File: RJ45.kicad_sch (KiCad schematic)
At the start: 5 parts, among them J9 RJ45_LED_Shielded

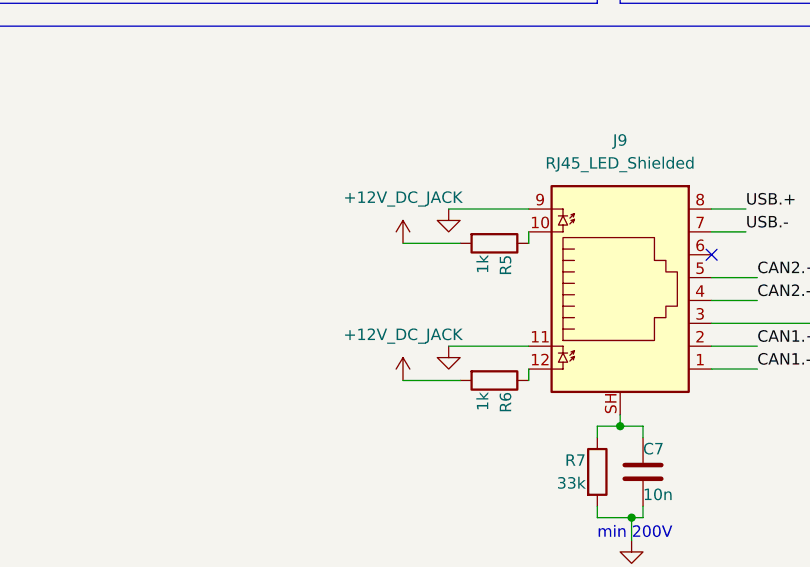
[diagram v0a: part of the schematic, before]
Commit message: Change power source
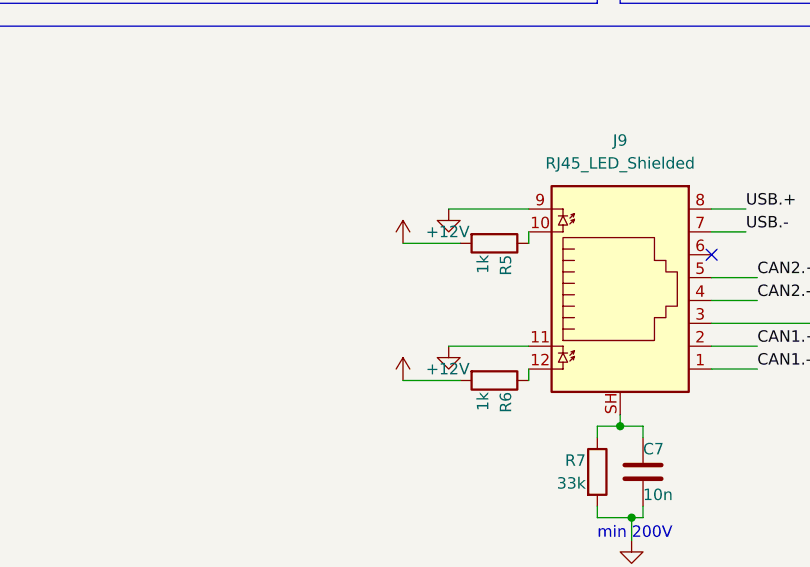
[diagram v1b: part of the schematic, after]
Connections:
- net +12V_DC_JACK renamed +12V
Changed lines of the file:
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@@
 			)
 		)
-		(property "Value" "+12V_DC_JACK"
-			(at 121.92 120.65 0)
+		(property "Value" "+12V"
+			(at 124.46 124.4599 0)
 			(effects
 				(font
 					(size 1.27 1.27)
 				)
+				(justify left)
 			)
 		)
@@
 			)
 		)
-		(property "Value" "+12V_DC_JACK"
-			(at 121.92 105.41 0)
+		(property "Value" "+12V"
+			(at 124.46 109.2199 0)
 			(effects
 				(font
 					(size 1.27 1.27)
 				)
+				(justify left)
 			)
 		)

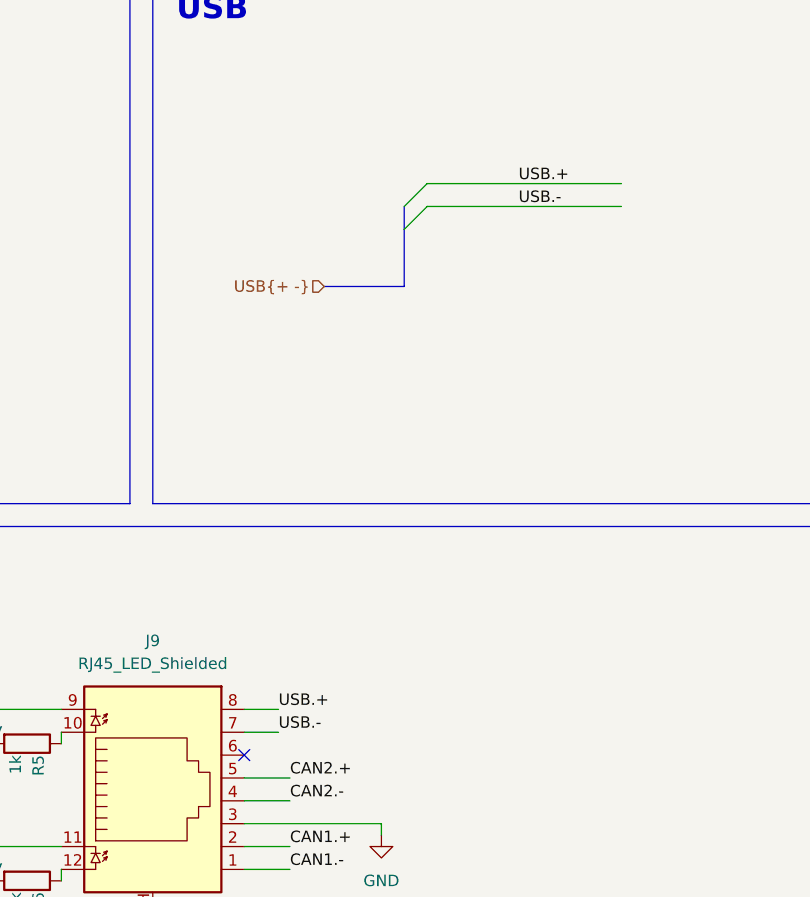
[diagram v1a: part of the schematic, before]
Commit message: Change USB net names
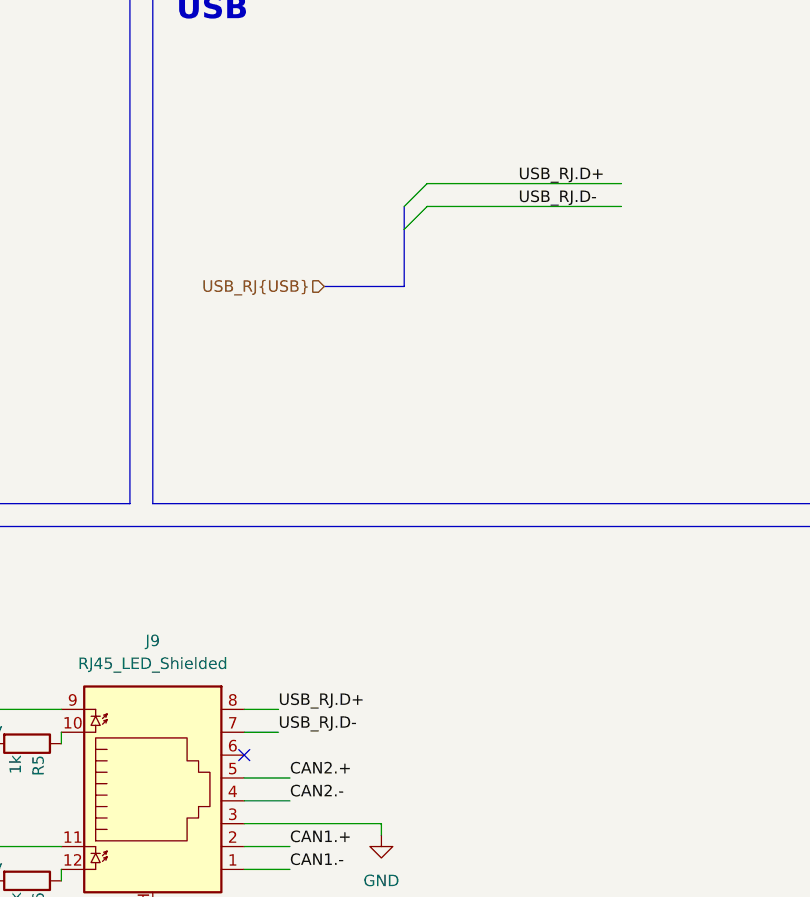
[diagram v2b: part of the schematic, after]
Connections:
- net USB.+ renamed USB_RJ.D+
- net USB.- renamed USB_RJ.D-
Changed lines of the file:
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@@
 		)
 	)
-	(label "USB.+"
+	(label "USB_RJ.D+"
 		(at 186.69 48.26 0)
 		(effects
@@
 		)
 	)
-	(label "USB.+"
+	(label "USB_RJ.D+"
 		(at 160.02 106.68 0)
 		(effects
@@
 		)
 	)
-	(label "USB.-"
-		(at 160.02 109.22 0)
+	(label "USB_RJ.D-"
+		(at 186.69 50.8 0)
 		(effects
 			(font
@@
 		)
 	)
-	(label "USB.-"
-		(at 186.69 50.8 0)
+	(label "USB_RJ.D-"
+		(at 160.02 109.22 0)
 		(effects
 			(font
@@
 		)
 	)
-	(hierarchical_label "USB{+ -}"
+	(hierarchical_label "USB_RJ{USB}"
 		(shape input)
 		(at 165.1 59.69 180)

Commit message: Fix USB connection
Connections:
- net USB_RJ.D+ renamed USB_RJ.+
- net USB_RJ.D- renamed USB_RJ.-
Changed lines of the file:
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@@
 		)
 	)
-	(label "USB_RJ.D+"
+	(label "USB_RJ.+"
 		(at 186.69 48.26 0)
 		(effects
@@
 		)
 	)
-	(label "USB_RJ.D+"
-		(at 160.02 106.68 0)
-		(effects
-			(font
-				(size 1.27 1.27)
-			)
-			(justify left bottom)
-		)
-	)
-	(label "USB_RJ.D-"
+	(label "USB_RJ.-"
 		(at 186.69 50.8 0)
 		(effects
@@
 		)
 	)
-	(label "USB_RJ.D-"
-		(at 160.02 109.22 0)
+	(label "USB_RJ.+"
+		(at 160.02 106.68 0)
 		(effects
 			(font
@@
 	(label "CAN2.+"
 		(at 161.29 114.3 0)
+		(effects
+			(font
+				(size 1.27 1.27)
+			)
+			(justify left bottom)
+		)
+	)
+	(label "USB_RJ.-"
+		(at 160.02 109.22 0)
 		(effects
 			(font
@@
 		)
 	)
-	(hierarchical_label "USB_RJ{USB}"
+	(hierarchical_label "USB_RJ{+ -}"
 		(shape input)
 		(at 165.1 59.69 180)

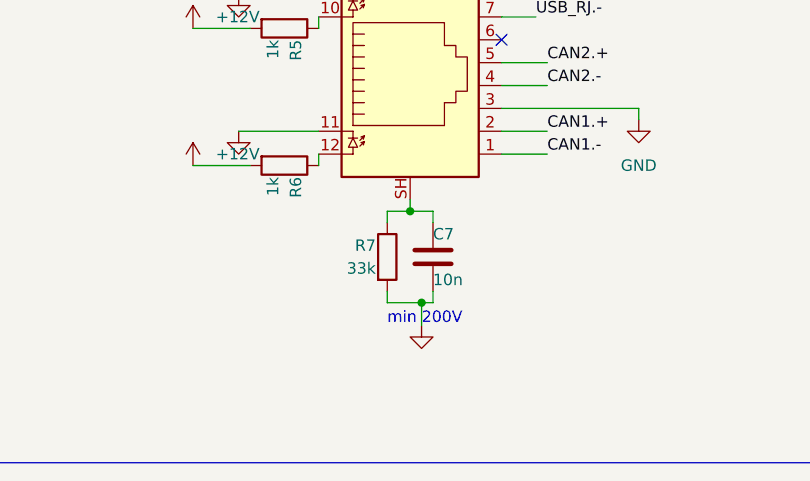
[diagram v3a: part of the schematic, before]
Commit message: Add extra capacitor and resistor
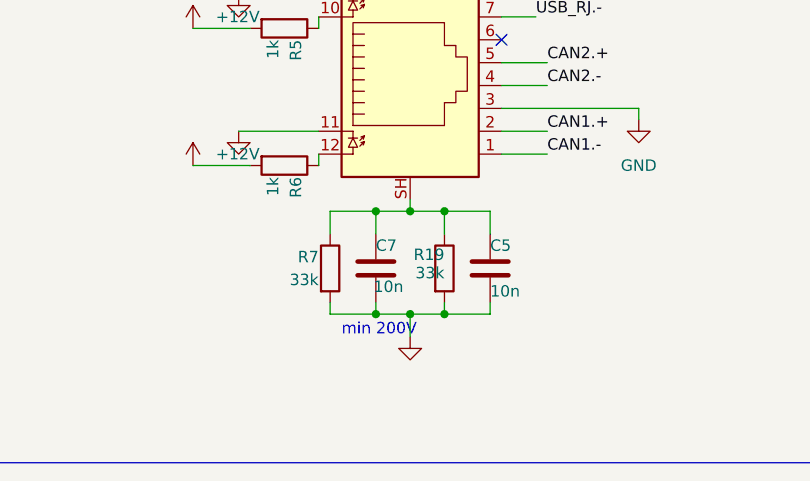
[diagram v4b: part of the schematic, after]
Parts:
- added C5: 10n, Capacitor_SMD:C_0402_1005Metric, symbol Device:C
- added R19: 33k, Resistor_SMD:R_0402_1005Metric, symbol Device:R
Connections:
- net GND: now also C5.2, R19.2
- net at C7.1, J9.SH, R7.1: now also C5.1, R19.1
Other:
- moved on the sheet: C7, R7
